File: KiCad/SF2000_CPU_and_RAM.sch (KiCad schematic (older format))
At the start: 1 part, among them U8 68000D

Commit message: more dev, added nets
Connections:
- net RW_3V3: now reaches U8.1 (R/~W)
- net RESET_3V3: now reaches U8.10 (~RESET)
- net AVEC_3V3: now reaches U8.11 (~AVEC)
- net A0_3V3: now reaches U8.19 (A0)
- net DTACK_CPU_3V3: now reaches U8.2 (~DTACK)
- net GND: now reaches U8.23 (GND)
- net GND: now also U8.56 (GND), U8.7 (GND)
- net BG_3V3: now reaches U8.3 (~BG)
- net BR_3V3: now reaches U8.4 (~BR)
- net 3V3: now reaches U8.41 (VCC)
- net 3V3: now also U8.5 (VCC), U8.8 (MODE)
- net D15_3V3: now reaches U8.45 (D15)
- net D14_3V3: now reaches U8.46 (D14)
- net D13_3V3: now reaches U8.47 (D13)
- net D12_3V3: now reaches U8.48 (D12)
- net D11_3V3: now reaches U8.49 (D11)
- net D10_3V3: now reaches U8.50 (D10)
- net D9_3V3: now reaches U8.51 (D9)
- net D8_3V3: now reaches U8.52 (D8)
- net D7_3V3: now reaches U8.53 (D7)
- net D6_3V3: now reaches U8.54 (D6)
- net D5_3V3: now reaches U8.55 (D5)
- net D4_3V3: now reaches U8.57 (D4)
- net D3_3V3: now reaches U8.58 (D3)
- net D2_3V3: now reaches U8.59 (D2)
- net D1_3V3: now reaches U8.60 (D1)
- net D0_3V3: now reaches U8.61 (D0)
- net AS_CPU_3V3: now reaches U8.62 (~AS)
- net UDS_3V3: now reaches U8.63 (~UDS)
- net LDS_3V3: now reaches U8.64 (~LDS)
- net HALT_3V3: now reaches U8.9 (~HALT)
- net CLKCPU renamed CLKCPU_3V3
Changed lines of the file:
@@
 U 1 1 621E09D7
 P 2500 3700
-F 0 "U8" H 2500 6281 50  0000 C CNN
-F 1 "68000D" H 2500 6190 50  0000 C CNN
+F 0 "U8" H 2500 3800 50  0000 C CNN
+F 1 "68000D" H 2500 3700 50  0000 C CNN
 F 2 "Package_QFP:LQFP-64_14x14mm_P0.8mm" H 2500 3700 50  0001 C CNN
 F 3 "https://www.nxp.com/docs/en/reference-manual/MC68000UM.pdf" H 2500 3700 50  0001 C CNN
@@
 $EndComp
 Text GLabel 1500 1500 0    50   Input ~ 0
-CLKCPU
+CLKCPU_3V3
 Text GLabel 3500 2000 2    50   Output ~ 0
 A5_3V3
@@
 Text GLabel 3500 3800 2    50   Output ~ 0
 A23_3V3
+Text GLabel 1500 2350 0    50   Output ~ 0
+BG_3V3
+Text GLabel 3500 1500 2    50   Output ~ 0
+A0_3V3
+Text GLabel 3500 3950 2    50   BiDi ~ 0
+D0_3V3
+Text GLabel 3500 4050 2    50   BiDi ~ 0
+D1_3V3
+Text GLabel 3500 4150 2    50   BiDi ~ 0
+D2_3V3
+Text GLabel 3500 4250 2    50   BiDi ~ 0
+D3_3V3
+Text GLabel 3500 4350 2    50   BiDi ~ 0
+D4_3V3
+Text GLabel 3500 4450 2    50   BiDi ~ 0
+D5_3V3
+Text GLabel 3500 4550 2    50   BiDi ~ 0
+D6_3V3
+Text GLabel 3500 4650 2    50   BiDi ~ 0
+D7_3V3
+Text GLabel 3500 4750 2    50   BiDi ~ 0
+D8_3V3
+Text GLabel 3500 4850 2    50   BiDi ~ 0
+D9_3V3
+Text GLabel 3500 4950 2    50   BiDi ~ 0
+D10_3V3
+Text GLabel 3500 5050 2    50   BiDi ~ 0
+D11_3V3
+Text GLabel 3500 5150 2    50   BiDi ~ 0
+D12_3V3
+Text GLabel 3500 5250 2    50   BiDi ~ 0
+D13_3V3
+Text GLabel 3500 5350 2    50   BiDi ~ 0
+D14_3V3
+Text GLabel 3500 5450 2    50   BiDi ~ 0
+D15_3V3
+Text GLabel 2500 1300 1    50   Input ~ 0
+3V3
+Wire Wire Line
+	2500 1300 2600 1300
+Text GLabel 1500 4700 0    50   Input ~ 0
+AVEC_3V3
+Text GLabel 1500 4800 0    50   BiDi ~ 0
+RESET_3V3
+Text GLabel 1500 4900 0    50   BiDi ~ 0
+HALT_3V3
+Text GLabel 1500 2450 0    50   Input ~ 0
+BR_3V3
+Text GLabel 1500 2250 0    50   Input ~ 0
+DTACK_CPU_3V3
+Text GLabel 2600 6100 3    50   Input ~ 0
+GND
+Wire Wire Line
+	2400 6100 2500 6100
+Connection ~ 2500 6100
+Wire Wire Line
+	2500 6100 2600 6100
+Text GLabel 3500 5600 2    50   Output ~ 0
+AS_CPU_3V3
+Text GLabel 3500 5700 2    50   Output ~ 0
+UDS_3V3
+Text GLabel 3500 5800 2    50   Output ~ 0
+LDS_3V3
+Text GLabel 3500 5900 2    50   Output ~ 0
+RW_3V3
+Text GLabel 1500 5000 0    50   Input ~ 0
+3V3
 $EndSCHEMATC

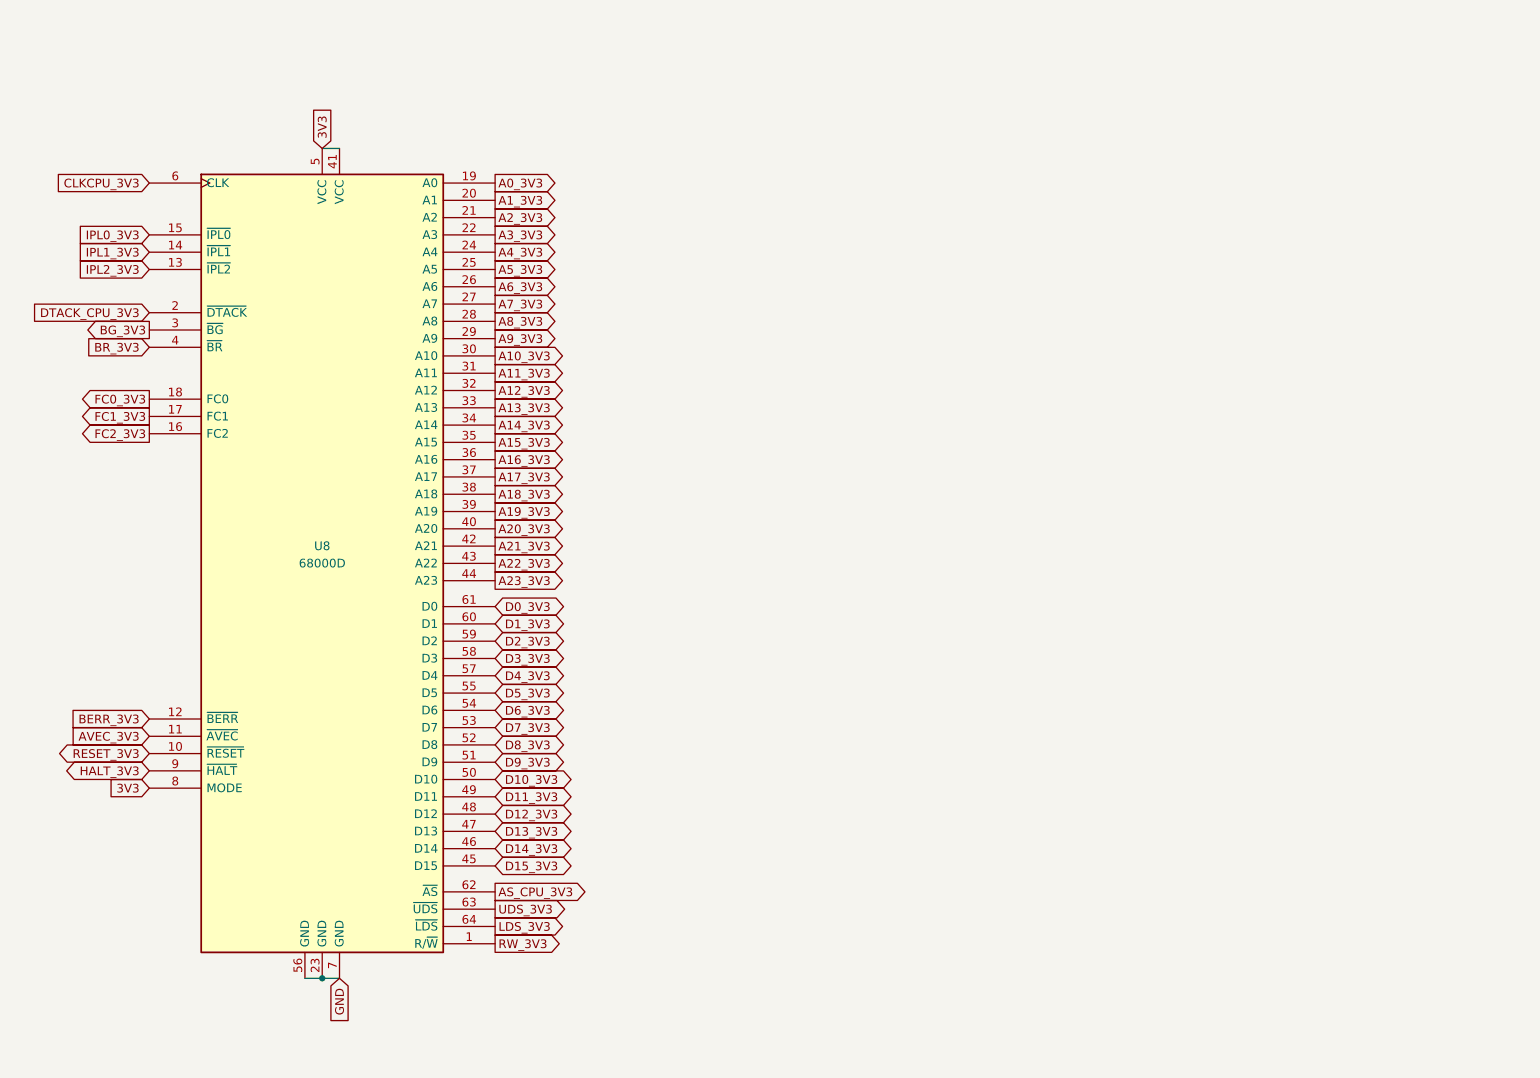
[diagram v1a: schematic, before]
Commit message: added SRAM-chips to the design
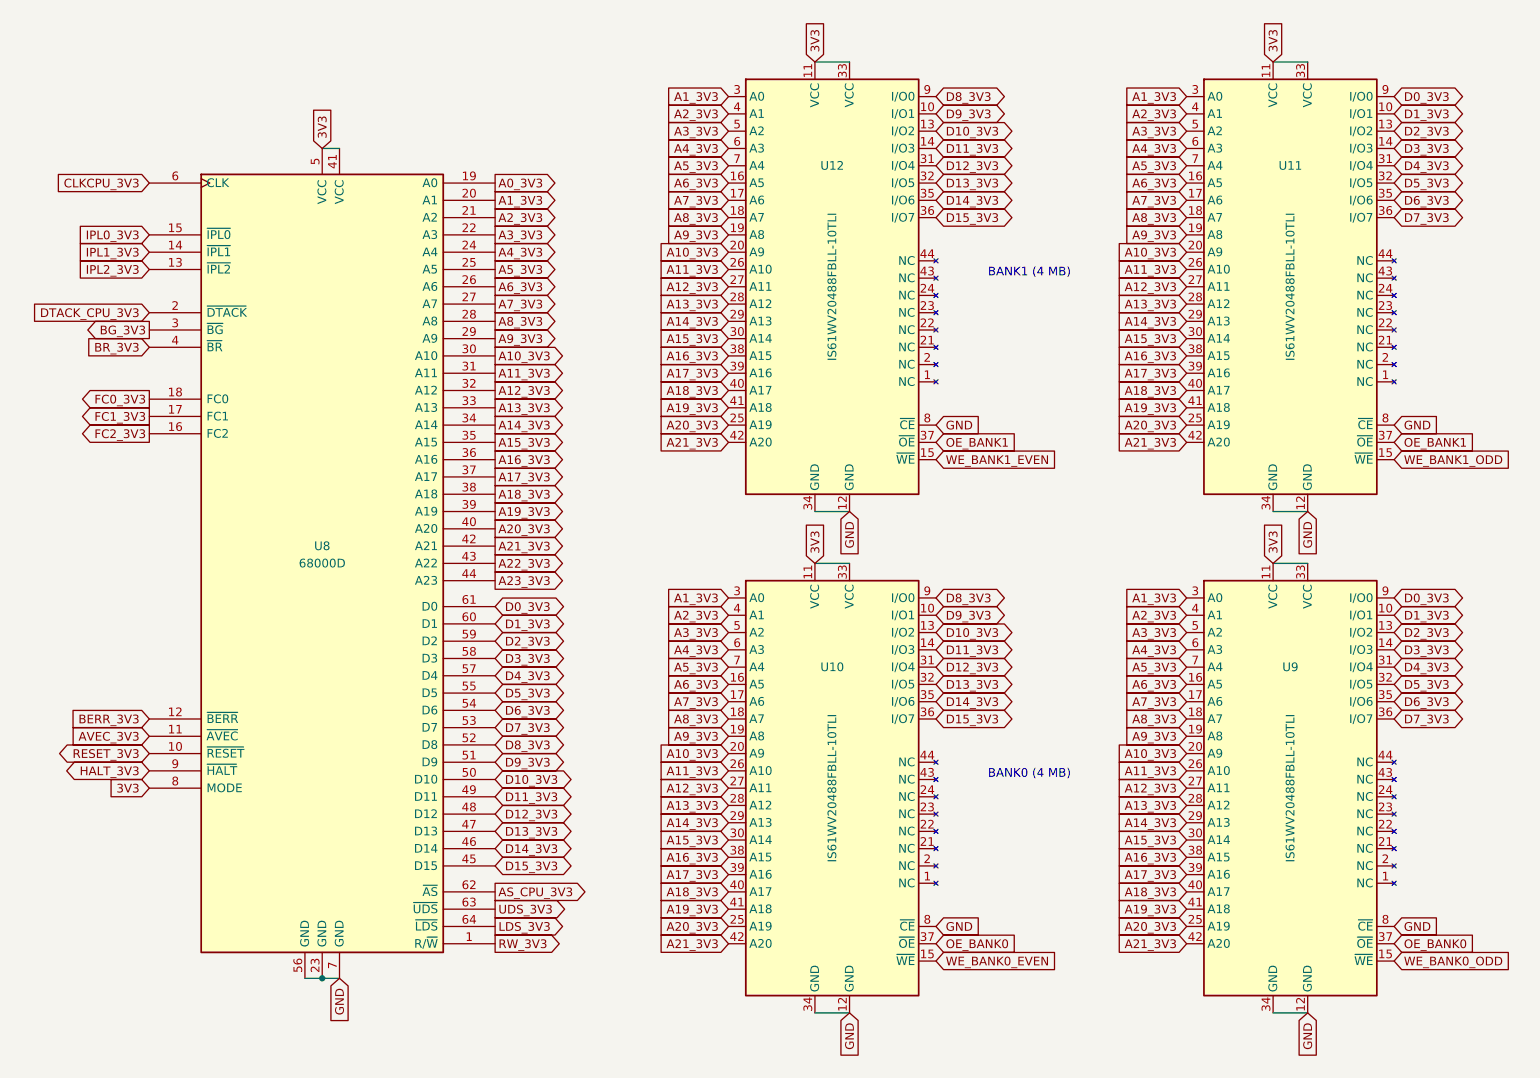
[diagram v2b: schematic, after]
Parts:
- added U10, U11, U12, U9: IS61WV20488FBLL-10TLI, Package_SO:TSOP-II-44_10.16x18.41mm_P0.8mm, symbol SF2000:IS61WV20488FBLL-10TLI
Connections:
- net 3V3: now also U10.11 (VCC), U10.33 (VCC), U11.11 (VCC), U11.33 (VCC), U12.11 (VCC), U12.33 (VCC), U9.11 (VCC), U9.33 (VCC)
- net A10_3V3: now also U10.20 (A9), U11.20 (A9), U12.20 (A9), U9.20 (A9)
- net A11_3V3: now also U10.26 (A10), U11.26 (A10), U12.26 (A10), U9.26 (A10)
- net A12_3V3: now also U10.27 (A11), U11.27 (A11), U12.27 (A11), U9.27 (A11)
- net A13_3V3: now also U10.28 (A12), U11.28 (A12), U12.28 (A12), U9.28 (A12)
- net A14_3V3: now also U10.29 (A13), U11.29 (A13), U12.29 (A13), U9.29 (A13)
- net A15_3V3: now also U10.30 (A14), U11.30 (A14), U12.30 (A14), U9.30 (A14)
- net A16_3V3: now also U10.38 (A15), U11.38 (A15), U12.38 (A15), U9.38 (A15)
- net A17_3V3: now also U10.39 (A16), U11.39 (A16), U12.39 (A16), U9.39 (A16)
- net A18_3V3: now also U10.40 (A17), U11.40 (A17), U12.40 (A17), U9.40 (A17)
- net A19_3V3: now also U10.41 (A18), U11.41 (A18), U12.41 (A18), U9.41 (A18)
- net A1_3V3: now also U10.3 (A0), U11.3 (A0), U12.3 (A0), U9.3 (A0)
- net A20_3V3: now also U10.25 (A19), U11.25 (A19), U12.25 (A19), U9.25 (A19)
- net A21_3V3: now also U10.42 (A20), U11.42 (A20), U12.42 (A20), U9.42 (A20)
- net A2_3V3: now also U10.4 (A1), U11.4 (A1), U12.4 (A1), U9.4 (A1)
- net A3_3V3: now also U10.5 (A2), U11.5 (A2), U12.5 (A2), U9.5 (A2)
- net A4_3V3: now also U10.6 (A3), U11.6 (A3), U12.6 (A3), U9.6 (A3)
- net A5_3V3: now also U10.7 (A4), U11.7 (A4), U12.7 (A4), U9.7 (A4)
- net A6_3V3: now also U10.16 (A5), U11.16 (A5), U12.16 (A5), U9.16 (A5)
- net A7_3V3: now also U10.17 (A6), U11.17 (A6), U12.17 (A6), U9.17 (A6)
- net A8_3V3: now also U10.18 (A7), U11.18 (A7), U12.18 (A7), U9.18 (A7)
- net A9_3V3: now also U10.19 (A8), U11.19 (A8), U12.19 (A8), U9.19 (A8)
- net D0_3V3: now also U11.9 (I/O0), U9.9 (I/O0)
- net D10_3V3: now also U10.13 (I/O2), U12.13 (I/O2)
- net D11_3V3: now also U10.14 (I/O3), U12.14 (I/O3)
- net D12_3V3: now also U10.31 (I/O4), U12.31 (I/O4)
- net D13_3V3: now also U10.32 (I/O5), U12.32 (I/O5)
- net D14_3V3: now also U10.35 (I/O6), U12.35 (I/O6)
- net D15_3V3: now also U10.36 (I/O7), U12.36 (I/O7)
- net D1_3V3: now also U11.10 (I/O1), U9.10 (I/O1)
- net D2_3V3: now also U11.13 (I/O2), U9.13 (I/O2)
- net D3_3V3: now also U11.14 (I/O3), U9.14 (I/O3)
- net D4_3V3: now also U11.31 (I/O4), U9.31 (I/O4)
- net D5_3V3: now also U11.32 (I/O5), U9.32 (I/O5)
- net D6_3V3: now also U11.35 (I/O6), U9.35 (I/O6)
- net D7_3V3: now also U11.36 (I/O7), U9.36 (I/O7)
- net D8_3V3: now also U10.9 (I/O0), U12.9 (I/O0)
- net D9_3V3: now also U10.10 (I/O1), U12.10 (I/O1)
- net GND: now also U10.12 (GND), U10.34 (GND), U10.8 (~CE), U11.12 (GND), U11.34 (GND), U11.8 (~CE), U12.12 (GND), U12.34 (GND), U12.8 (~CE), U9.12 (GND), U9.34 (GND), U9.8 (~CE)
- new net OE_BANK0: U10.37 (~OE), U9.37 (~OE)
- new net OE_BANK1: U11.37 (~OE), U12.37 (~OE)
- new net WE_BANK0_EVEN: U10.15 (~WE)
- new net WE_BANK0_ODD: U9.15 (~WE)
- new net WE_BANK1_EVEN: U12.15 (~WE)
- new net WE_BANK1_ODD: U11.15 (~WE)
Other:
- note added: "BANK0 (4 MB)"
- note added: "BANK1 (4 MB)"
